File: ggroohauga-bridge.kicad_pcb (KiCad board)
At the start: 2 copper layers, 101.6 x 31 mm, 6 parts

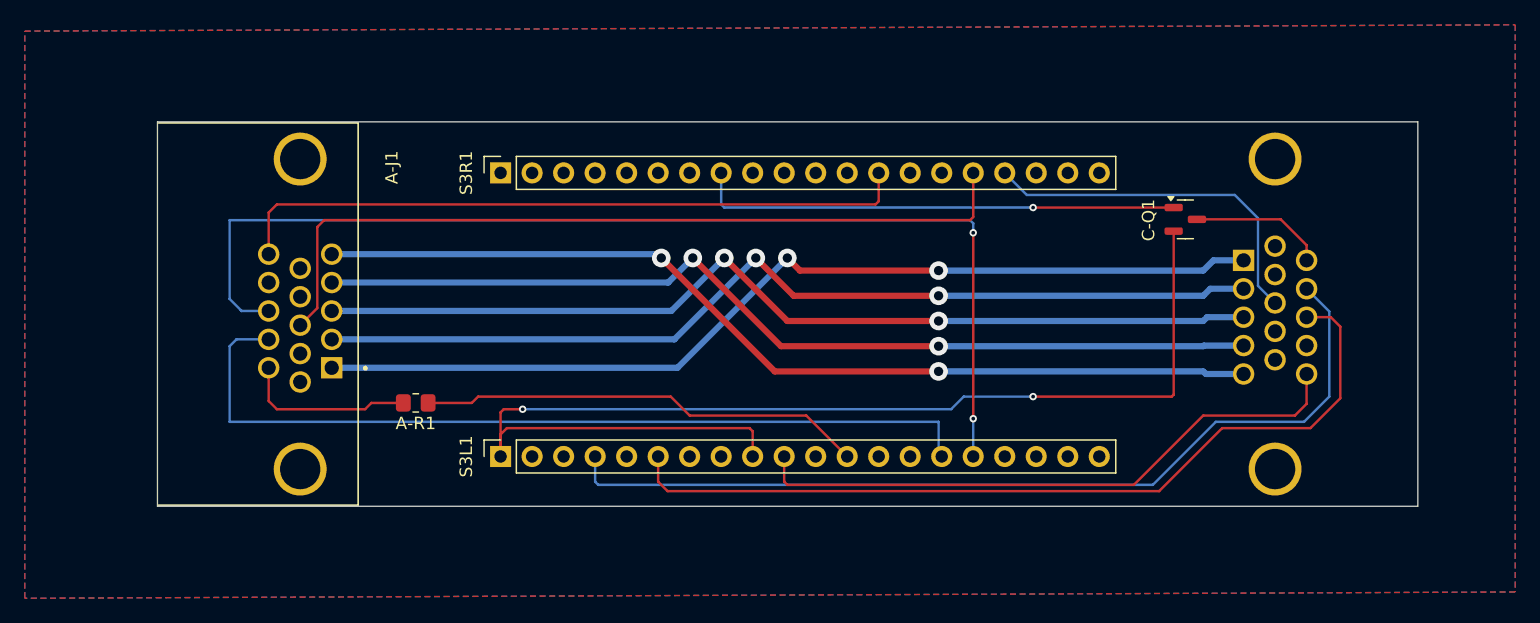
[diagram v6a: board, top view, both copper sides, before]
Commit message: Add 4ch digital isolator to the bridge PCB
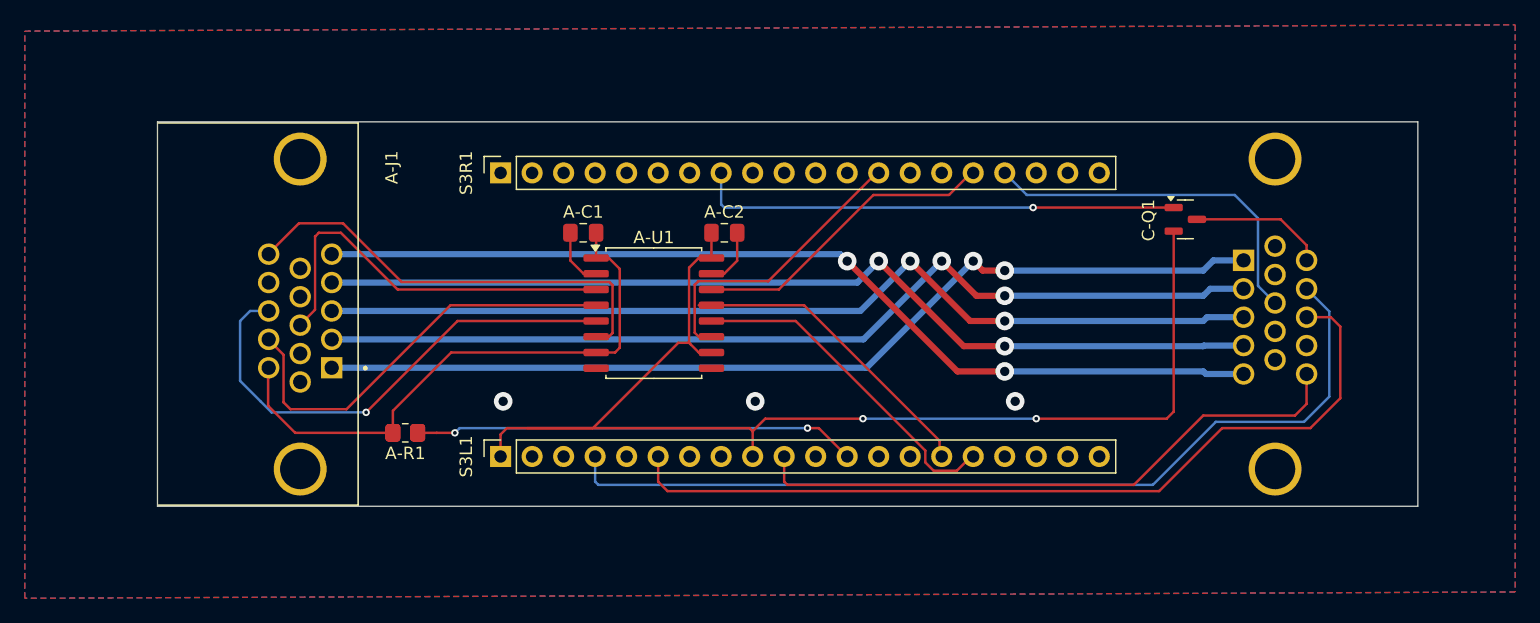
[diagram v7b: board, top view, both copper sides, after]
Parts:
- added ?: , , F.Cu at (74.9, 75.6)
- added ?: , , F.Cu at (72.9, 75.6)
- added A-C1: 0.1µF, Capacitor_SMD:C_0805_2012Metric_Pad1.18x1.45mm_HandSolder, F.Cu at (88.2, 59.4)
- added A-C2: 0.1µF, Capacitor_SMD:C_0805_2012Metric_Pad1.18x1.45mm_HandSolder, F.Cu at (99.6, 59.4)
- added A-U1: ISO6742, Package_SO:SOIC-16W_7.5x10.3mm_P1.27mm, F.Cu at (93.9, 65.9)
- moved A-R1 2.56 mm to (73.9, 75.6)
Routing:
- net (no net): track 278.7 -> 0.00 mm, vias 2 -> 0
- net /Common/AMP_RX: track 0.00 -> 40.2 mm, vias 0 -> 1
- net /Common/CON_ANNOUNCE: track 0.00 -> 36.2 mm
- net /Common/AMP_TX: track 0.00 -> 34.5 mm
- net /Common/AMP_POWER_IN: track 14.0 -> 47.5 mm
- net /Common/AMP_DETECT: track 0.00 -> 32.3 mm
- net /Common/GPIO_L10_C10_M14/AMP_RX: track 0.00 -> 27.0 mm
- net /Common/GPIO_L9_C9_M13/AMP_TX: track 0.00 -> 25.2 mm
- net /Common/GPIO_L14_C48_M33/AMP_DETECT: track 0.00 -> 24.8 mm
- net /Common/GPIO_L48_C35_M36/CON_ANNOUNCE: track 0.00 -> 23.7 mm
- net GND: track 0.00 -> 9.52 mm, vias 0 -> 3
- net +3.3V: track 96.0 -> 101.9 mm
- net /Common/GPIO_L8_C8_M10/AMP_POWER_IN: track 36.0 -> 35.7 mm, vias 0 -> 2

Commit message: Ground unused GPIOs
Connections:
- A-C1 pad 2: GND -> GPIO_L11_C11_M15
- A-C2 pad 2: GND -> GPIO_L11_C11_M15
- A-J1 pad 0: GND -> GPIO_L11_C11_M15
- A-J1 pad 6: GND -> GPIO_L11_C11_M15
- A-U1 pad 15: GND -> GPIO_L11_C11_M15
- A-U1 pad 2: GND -> GPIO_L11_C11_M15
- A-U1 pad 8: GND -> GPIO_L11_C11_M15
- A-U1 pad 9: GND -> GPIO_L11_C11_M15
- C-J1 pad 0: GND -> GPIO_L11_C11_M15
- C-J1 pad 6: GND -> GPIO_L11_C11_M15
- S3L1 pad 11: GPIO_L18_C18_M9 -> GPIO_L11_C11_M15
- S3L1 pad 18: GPIO_L12_C12_M16 -> GPIO_L11_C11_M15
- S3L1 pad 7: GND -> GPIO_L11_C11_M15
- S3L1 pad 8: GND -> GPIO_L11_C11_M15
- S3R1 pad 1: GND -> GPIO_L11_C11_M15
- S3R1 pad 14: GPIO_L47_C47_M35 -> GPIO_L11_C11_M15
- S3R1 pad 15: GPIO_L21_C21_M21 -> GPIO_L11_C11_M15
- S3R1 pad 7: GPIO_L41_C41_M42 -> GPIO_L11_C11_M15
- S3R1 pad 9: GPIO_L39_C39_M40 -> GPIO_L11_C11_M15
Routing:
- net GPIO_L11_C11_M15: track 0.00 -> 9.52 mm, vias 0 -> 3
- net GND: track 9.52 -> 0.00 mm, vias 3 -> 0
- added copper zone on B.Cu, net GPIO_L11_C11_M15
- added copper zone on F.Cu, net GPIO_L11_C11_M15
- removed copper zone on B.Cu, net GND
- removed copper zone on F.Cu, net GND
